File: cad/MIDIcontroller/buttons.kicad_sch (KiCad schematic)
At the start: 16 parts, among them SW1 SW_SPST, SW2 SW_SPST, SW3 SW_SPST, SW4 SW_SPST

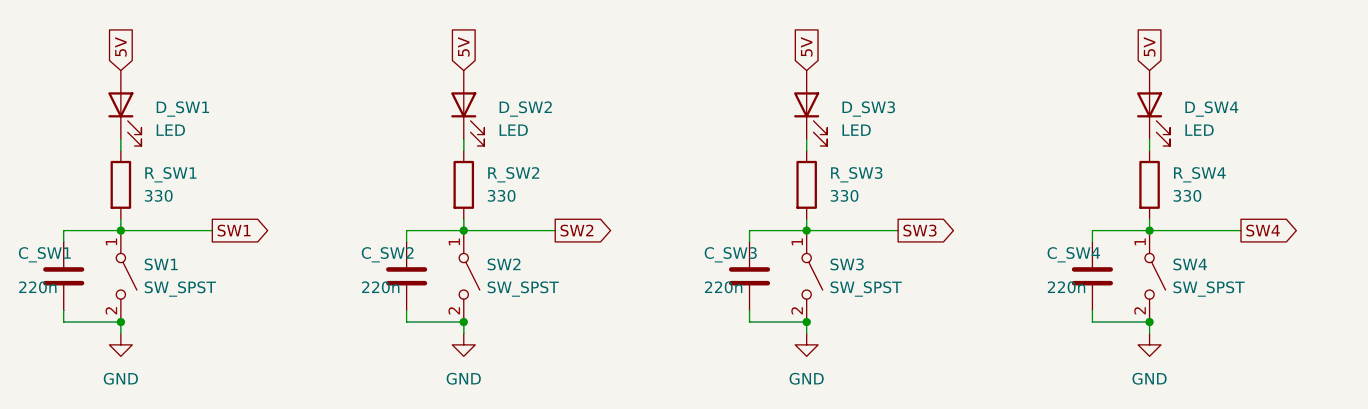
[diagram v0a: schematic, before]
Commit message: Added button on encoder
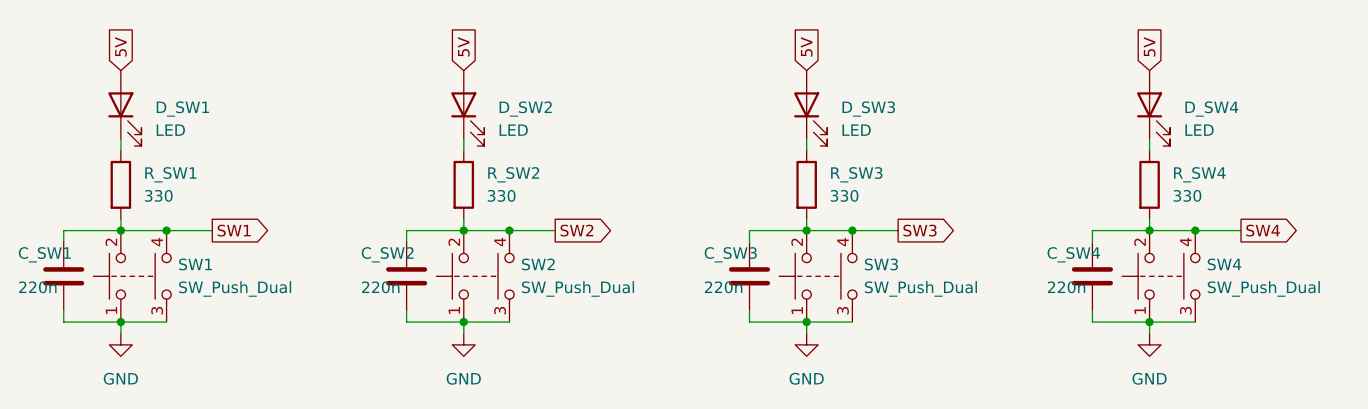
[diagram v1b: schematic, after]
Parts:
- removed SW1, SW2, SW3, SW4: SW_SPST, Button_Switch_THT:SW_SPST_Omron_B3F-315x_Angled, symbol Switch:SW_SPST
- added SW1, SW2, SW3, SW4: SW_Push_Dual, Button_Switch_THT:SW_PUSH_6mm_H5mm, symbol Switch:SW_Push_Dual
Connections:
- net GND: now also SW1.1, SW1.3, SW2.1, SW2.3, SW3.1, SW3.3, SW4.1, SW4.3
- net SW1: now also SW1.2, SW1.4
- net SW2: now also SW2.2, SW2.4
- net SW3: now also SW3.2, SW3.4
- net SW4: now also SW4.2, SW4.4
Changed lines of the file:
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@@
   (junction (at 207.01 104.14) (diameter 0) (color 0 0 0 0)
   )
+  (junction (at 207.01 114.3) (diameter 0) (color 0 0 0 0)
+  )
+  (junction (at 92.71 114.3) (diameter 0) (color 0 0 0 0)
+  )
+  (junction (at 212.09 104.14) (diameter 0) (color 0 0 0 0)
+  )
+  (junction (at 97.79 104.14) (diameter 0) (color 0 0 0 0)
+  )
+  (junction (at 135.89 104.14) (diameter 0) (color 0 0 0 0)
+  )
+  (junction (at 168.91 104.14) (diameter 0) (color 0 0 0 0)
+  )
+  (junction (at 92.71 104.14) (diameter 0) (color 0 0 0 0)
+  )
   (junction (at 168.91 114.3) (diameter 0) (color 0 0 0 0)
   )
-  (junction (at 168.91 104.14) (diameter 0) (color 0 0 0 0)
-  )
-  (junction (at 92.71 114.3) (diameter 0) (color 0 0 0 0)
-  )
-  (junction (at 207.01 114.3) (diameter 0) (color 0 0 0 0)
-  )
-  (junction (at 92.71 104.14) (diameter 0) (color 0 0 0 0)
+  (junction (at 173.99 104.14) (diameter 0) (color 0 0 0 0)
   )
   (junction (at 130.81 114.3) (diameter 0) (color 0 0 0 0)
@@
     (stroke (width 0) (type default) (color 0 0 0 0))
   )
-  (wire (pts (xy 92.71 104.14) (xy 102.87 104.14))
+  (wire (pts (xy 207.01 114.3) (xy 212.09 114.3))
     (stroke (width 0) (type default) (color 0 0 0 0))
   )
@@
     (stroke (width 0) (type default) (color 0 0 0 0))
   )
+  (wire (pts (xy 168.91 114.3) (xy 173.99 114.3))
+    (stroke (width 0) (type default) (color 0 0 0 0))
+  )
+  (wire (pts (xy 92.71 114.3) (xy 97.79 114.3))
+    (stroke (width 0) (type default) (color 0 0 0 0))
+  )
   (wire (pts (xy 168.91 114.3) (xy 168.91 115.57))
     (stroke (width 0) (type default) (color 0 0 0 0))
@@
     (stroke (width 0) (type default) (color 0 0 0 0))
   )
-  (wire (pts (xy 168.91 104.14) (xy 179.07 104.14))
+  (wire (pts (xy 97.79 104.14) (xy 102.87 104.14))
+    (stroke (width 0) (type default) (color 0 0 0 0))
+  )
+  (wire (pts (xy 92.71 104.14) (xy 97.79 104.14))
+    (stroke (width 0) (type default) (color 0 0 0 0))
+  )
+  (wire (pts (xy 168.91 104.14) (xy 173.99 104.14))
     (stroke (width 0) (type default) (color 0 0 0 0))
   )
@@
     (stroke (width 0) (type default) (color 0 0 0 0))
   )
-  (wire (pts (xy 130.81 104.14) (xy 140.97 104.14))
+  (wire (pts (xy 130.81 114.3) (xy 135.89 114.3))
+    (stroke (width 0) (type default) (color 0 0 0 0))
+  )
+  (wire (pts (xy 173.99 104.14) (xy 179.07 104.14))
     (stroke (width 0) (type default) (color 0 0 0 0))
   )
@@
     (stroke (width 0) (type default) (color 0 0 0 0))
   )
-  (wire (pts (xy 207.01 104.14) (xy 217.17 104.14))
-    (stroke (width 0) (type default) (color 0 0 0 0))
-  )
   (wire (pts (xy 86.36 114.3) (xy 92.71 114.3))
     (stroke (width 0) (type default) (color 0 0 0 0))
   )
+  (wire (pts (xy 207.01 104.14) (xy 212.09 104.14))
+    (stroke (width 0) (type default) (color 0 0 0 0))
+  )
   (wire (pts (xy 130.81 93.98) (xy 130.81 95.25))
     (stroke (width 0) (type default) (color 0 0 0 0))
   )
+  (wire (pts (xy 130.81 104.14) (xy 135.89 104.14))
+    (stroke (width 0) (type default) (color 0 0 0 0))
+  )
   (wire (pts (xy 86.36 104.14) (xy 92.71 104.14))
     (stroke (width 0) (type default) (color 0 0 0 0))
   )
+  (wire (pts (xy 135.89 104.14) (xy 140.97 104.14))
+    (stroke (width 0) (type default) (color 0 0 0 0))
+  )
   (wire (pts (xy 200.66 105.41) (xy 200.66 104.14))
     (stroke (width 0) (type default) (color 0 0 0 0))
@@
     (stroke (width 0) (type default) (color 0 0 0 0))
   )
+  (wire (pts (xy 212.09 104.14) (xy 217.17 104.14))
+    (stroke (width 0) (type default) (color 0 0 0 0))
+  )
   (wire (pts (xy 124.46 114.3) (xy 130.81 114.3))
     (stroke (width 0) (type default) (color 0 0 0 0))
@@
     )
   )
-  (symbol (lib_id "Switch:SW_SPST") (at 168.91 109.22 270) (unit 1)
-    (in_bom yes) (on_board yes) (fields_autoplaced)
-    (property "Reference" "SW3" (id 0) (at 171.45 107.9499 90)
-      (effects (font (size 1.27 1.27)) (justify left))
-    )
-    (property "Value" "SW_SPST" (id 1) (at 171.45 110.4899 90)
-      (effects (font (size 1.27 1.27)) (justify left))
-    )
-    (property "Footprint" "Button_Switch_THT:SW_SPST_Omron_B3F-315x_Angled" (id 2) (at 168.91 109.22 0)
-      (effects (font (size 1.27 1.27)) hide)
-    )
-    (property "Datasheet" "~" (id 3) (at 168.91 109.22 0)
-      (effects (font (size 1.27 1.27)) hide)
-    )
-    (pin "1")
-    (pin "2")
+  (symbol (lib_id "Switch:SW_Push_Dual") (at 130.81 109.22 90) (unit 1)
+    (in_bom yes) (on_board yes) (fields_autoplaced)
+    (property "Reference" "SW2" (id 0) (at 137.16 107.9499 90)
+      (effects (font (size 1.27 1.27)) (justify right))
+    )
+    (property "Value" "SW_Push_Dual" (id 1) (at 137.16 110.4899 90)
+      (effects (font (size 1.27 1.27)) (justify right))
+    )
+    (property "Footprint" "Button_Switch_THT:SW_PUSH_6mm_H5mm" (id 2) (at 125.73 109.22 0)
+      (effects (font (size 1.27 1.27)) hide)
+    )
+    (property "Datasheet" "~" (id 3) (at 125.73 109.22 0)
+      (effects (font (size 1.27 1.27)) hide)
+    )
+    (pin "1")
+    (pin "2")
+    (pin "3")
+    (pin "4")
   )
   (symbol (lib_id "power:GND") (at 168.91 115.57 0) (unit 1)
@@
     (pin "1")
   )
+  (symbol (lib_id "Switch:SW_Push_Dual") (at 207.01 109.22 90) (unit 1)
+    (in_bom yes) (on_board yes) (fields_autoplaced)
+    (property "Reference" "SW4" (id 0) (at 213.36 107.9499 90)
+      (effects (font (size 1.27 1.27)) (justify right))
+    )
+    (property "Value" "SW_Push_Dual" (id 1) (at 213.36 110.4899 90)
+      (effects (font (size 1.27 1.27)) (justify right))
+    )
+    (property "Footprint" "Button_Switch_THT:SW_PUSH_6mm_H5mm" (id 2) (at 201.93 109.22 0)
+      (effects (font (size 1.27 1.27)) hide)
+    )
+    (property "Datasheet" "~" (id 3) (at 201.93 109.22 0)
+      (effects (font (size 1.27 1.27)) hide)
+    )
+    (pin "1")
+    (pin "2")
+    (pin "3")
+    (pin "4")
+  )
   (symbol (lib_id "Device:LED") (at 168.91 90.17 90) (unit 1)
     (in_bom yes) (on_board yes) (fields_autoplaced)
@@
     )
     (property "Datasheet" "~" (id 3) (at 168.91 90.17 0)
-      (effects (font (size 1.27 1.27)) hide)
-    )
-    (pin "1")
-    (pin "2")
-  )
-  (symbol (lib_id "Switch:SW_SPST") (at 92.71 109.22 270) (unit 1)
-    (in_bom yes) (on_board yes) (fields_autoplaced)
-    (property "Reference" "SW1" (id 0) (at 95.25 107.9499 90)
-      (effects (font (size 1.27 1.27)) (justify left))
-    )
-    (property "Value" "SW_SPST" (id 1) (at 95.25 110.4899 90)
-      (effects (font (size 1.27 1.27)) (justify left))
-    )
-    (property "Footprint" "Button_Switch_THT:SW_SPST_Omron_B3F-315x_Angled" (id 2) (at 92.71 109.22 0)
-      (effects (font (size 1.27 1.27)) hide)
-    )
-    (property "Datasheet" "~" (id 3) (at 92.71 109.22 0)
       (effects (font (size 1.27 1.27)) hide)
     )
@@
     )
     (pin "1")
+  )
+  (symbol (lib_id "Switch:SW_Push_Dual") (at 92.71 109.22 90) (unit 1)
+    (in_bom yes) (on_board yes) (fields_autoplaced)
+    (property "Reference" "SW1" (id 0) (at 99.06 107.9499 90)
+      (effects (font (size 1.27 1.27)) (justify right))
+    )
+    (property "Value" "SW_Push_Dual" (id 1) (at 99.06 110.4899 90)
+      (effects (font (size 1.27 1.27)) (justify right))
+    )
+    (property "Footprint" "Button_Switch_THT:SW_PUSH_6mm_H5mm" (id 2) (at 87.63 109.22 0)
+      (effects (font (size 1.27 1.27)) hide)
+    )
+    (property "Datasheet" "~" (id 3) (at 87.63 109.22 0)
+      (effects (font (size 1.27 1.27)) hide)
+    )
+    (pin "1")
+    (pin "2")
+    (pin "3")
+    (pin "4")
   )
   (symbol (lib_id "Device:LED") (at 92.71 90.17 90) (unit 1)
@@
     (pin "2")
   )
+  (symbol (lib_id "Switch:SW_Push_Dual") (at 168.91 109.22 90) (unit 1)
+    (in_bom yes) (on_board yes) (fields_autoplaced)
+    (property "Reference" "SW3" (id 0) (at 175.26 107.9499 90)
+      (effects (font (size 1.27 1.27)) (justify right))
+    )
+    (property "Value" "SW_Push_Dual" (id 1) (at 175.26 110.4899 90)
+      (effects (font (size 1.27 1.27)) (justify right))
+    )
+    (property "Footprint" "Button_Switch_THT:SW_PUSH_6mm_H5mm" (id 2) (at 163.83 109.22 0)
+      (effects (font (size 1.27 1.27)) hide)
+    )
+    (property "Datasheet" "~" (id 3) (at 163.83 109.22 0)
+      (effects (font (size 1.27 1.27)) hide)
+    )
+    (pin "1")
+    (pin "2")
+    (pin "3")
+    (pin "4")
+  )
   (symbol (lib_id "Device:LED") (at 130.81 90.17 90) (unit 1)
     (in_bom yes) (on_board yes) (fields_autoplaced)
@@
     (pin "2")
   )
-  (symbol (lib_id "Switch:SW_SPST") (at 130.81 109.22 270) (unit 1)
-    (in_bom yes) (on_board yes) (fields_autoplaced)
-    (property "Reference" "SW2" (id 0) (at 133.35 107.9499 90)
-      (effects (font (size 1.27 1.27)) (justify left))
-    )
-    (property "Value" "SW_SPST" (id 1) (at 133.35 110.4899 90)
-      (effects (font (size 1.27 1.27)) (justify left))
-    )
-    (property "Footprint" "Button_Switch_THT:SW_SPST_Omron_B3F-315x_Angled" (id 2) (at 130.81 109.22 0)
-      (effects (font (size 1.27 1.27)) hide)
-    )
-    (property "Datasheet" "~" (id 3) (at 130.81 109.22 0)
-      (effects (font (size 1.27 1.27)) hide)
-    )
-    (pin "1")
-    (pin "2")
-  )
   (symbol (lib_id "Device:R") (at 92.71 99.06 0) (unit 1)
     (in_bom yes) (on_board yes) (fields_autoplaced)
@@
       (effects (font (size 1.27 1.27)) hide)
     )
-    (pin "1")
-    (pin "2")
-  )
-  (symbol (lib_id "Switch:SW_SPST") (at 207.01 109.22 270) (unit 1)
-    (in_bom yes) (on_board yes) (fields_autoplaced)
-    (property "Reference" "SW4" (id 0) (at 209.55 107.9499 90)
-      (effects (font (size 1.27 1.27)) (justify left))
-    )
-    (property "Value" "SW_SPST" (id 1) (at 209.55 110.4899 90)
-      (effects (font (size 1.27 1.27)) (justify left))
-    )
-    (property "Footprint" "Button_Switch_THT:SW_SPST_Omron_B3F-315x_Angled" (id 2) (at 207.01 109.22 0)
-      (effects (font (size 1.27 1.27)) hide)
-    )
-    (property "Datasheet" "~" (id 3) (at 207.01 109.22 0)
-      (effects (font (size 1.27 1.27)) hide)
-    )
